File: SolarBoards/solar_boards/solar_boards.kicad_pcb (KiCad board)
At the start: 2 copper layers, 51.8 x 47 mm, 5 parts, among them J1 M55-6001242R

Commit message: boost converter values, will add solar cell
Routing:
- net (no net): track 0.00 -> 15.2 mm
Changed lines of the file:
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@@
 		(layer "Edge.Cuts")
+	)
+	(segment
+		(start 98 83.5)
+		(end 87 83.5)
+		(width 0.2)
+		(layer "F.Cu")
+		(net 0)
+	)
+	(segment
+		(start 87 83.5)
+		(end 84 86.5)
+		(width 0.2)
+		(layer "F.Cu")
+		(net 0)
 	)
 	(embedded_fonts no)

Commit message: Solar Board Schematic and Routing
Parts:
- added C1: 10uF, Capacitor_SMD:C_0402_1005Metric_Pad0.74x0.62mm_HandSolder, B.Cu at (89.1, 86.4)
- added C2: 10uF, Capacitor_SMD:C_0402_1005Metric_Pad0.74x0.62mm_HandSolder, B.Cu at (89.1, 87.8)
- added C3: 10uF, Capacitor_SMD:C_0402_1005Metric_Pad0.74x0.62mm_HandSolder, B.Cu at (93.7, 92.8)
- added C4: 1uF, Capacitor_SMD:C_0402_1005Metric_Pad0.74x0.62mm_HandSolder, B.Cu at (89.7, 93.8)
- added C5: 4.7uF, Capacitor_SMD:C_0402_1005Metric_Pad0.74x0.62mm_HandSolder, B.Cu at (83.5, 91.1)
- added C6: 10uF, Capacitor_SMD:C_0402_1005Metric_Pad0.74x0.62mm_HandSolder, B.Cu at (95.3, 92.8)
- added C7: 100nF, Capacitor_SMD:C_0402_1005Metric_Pad0.74x0.62mm_HandSolder, B.Cu at (96.9, 97.1)
- added C8: 1uF, Capacitor_SMD:C_0402_1005Metric_Pad0.74x0.62mm_HandSolder, B.Cu at (97.5, 92.8)
- added C9: 1uF, Capacitor_SMD:C_0402_1005Metric_Pad0.74x0.62mm_HandSolder, B.Cu at (101.2, 92.7)
- added D1: CDBQC0130L, inspireFly:DIODFN100X60X55-2N, F.Cu at (75.2, 74.5)
- added D2: CDBQC0130L, inspireFly:DIODFN100X60X55-2N, F.Cu at (84.6, 83.8)
- added D3: CDBQC0130L, inspireFly:DIODFN100X60X55-2N, F.Cu at (84.6, 92.6)
- added D4: CDBQC0130L, inspireFly:DIODFN100X60X55-2N, F.Cu at (84.6, 102.3)
- added D5: CDBQC0130L, inspireFly:DIODFN100X60X55-2N, F.Cu at (93.2, 76.0)
- added D6: CDBQC0130L, inspireFly:DIODFN100X60X55-2N, F.Cu at (99.2, 76.0)
- added L1: 10uH, inspireFly:WE-LQFS_3818, B.Cu at (94.0, 88.2)
- added R1: 332K, Resistor_SMD:R_0402_1005Metric_Pad0.72x0.64mm_HandSolder, B.Cu at (83.5, 89.6)
- added R2: 820K, Resistor_SMD:R_0402_1005Metric_Pad0.72x0.64mm_HandSolder, B.Cu at (91.4, 92.8)
- added R3: 200K, Resistor_SMD:R_0402_1005Metric_Pad0.72x0.64mm_HandSolder, B.Cu at (91.4, 95.6)
- added R4: 549K, Resistor_SMD:R_0402_1005Metric_Pad0.72x0.64mm_HandSolder, B.Cu at (98.0, 87.0)
- added R5: 200K, Resistor_SMD:R_0402_1005Metric_Pad0.72x0.64mm_HandSolder, B.Cu at (98.0, 84.8)
- added R6: 200K, Resistor_SMD:R_0402_1005Metric_Pad0.72x0.64mm_HandSolder, B.Cu at (102.1, 84.8)
- added R7: 820K, Resistor_SMD:R_0402_1005Metric_Pad0.72x0.64mm_HandSolder, B.Cu at (102.1, 87.0)
- added SC1: Solar_Cell, inspireFly:SOLAR_KXOB25-14X1F-TR, F.Cu at (71.8, 79.5)
- added SC2: Solar_Cell, inspireFly:SOLAR_KXOB25-14X1F-TR, F.Cu at (71.8, 88.2)
- added SC3: Solar_Cell, inspireFly:SOLAR_KXOB25-14X1F-TR, F.Cu at (71.7, 96.8)
- added SC4: Solar_Cell, inspireFly:SOLAR_KXOB25-14X1F-TR, F.Cu at (71.5, 105.5)
- added SC5: Solar_Cell, inspireFly:SOLAR_KXOB25-14X1F-TR, F.Cu at (97.8, 81.4)
- added SC6: Solar_Cell, inspireFly:SOLAR_KXOB25-14X1F-TR, F.Cu at (97.8, 104.2)
- added U1: LTC3105EDD-TRPBF, inspireFly:DFN-10_DD_LIT, B.Cu at (88.2, 90.6)
- added U2: OPT3004DNPR, inspireFly:DNP0006A, F.Cu at (99.0, 95.1)
- added U3: LM73100RPWR, inspireFly:IC_LM73100RPWR, B.Cu at (99.9, 90.1)
- moved J1 0.61 mm to (108.1, 92.6), turned to -90 degrees
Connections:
- J1 pad A1: unconnected-(J1-PadA1) -> GND
- J1 pad A2: unconnected-(J1-PadA2) -> GND
- J1 pad A3: unconnected-(J1-PadA3) -> GND
- J1 pad A4: unconnected-(J1-PadA4) -> GND
- J1 pad A5: unconnected-(J1-PadA5) -> GND
- J1 pad A6: unconnected-(J1-PadA6) -> GND
- J1 pad B1: unconnected-(J1-PadB1) -> EXTERNAL_VOLTAGE
- J1 pad B2: unconnected-(J1-PadB2) -> EXTERNAL_VOLTAGE
- J1 pad B3: unconnected-(J1-PadB3) -> EXTERNAL_VOLTAGE
- J1 pad B4: unconnected-(J1-PadB4) -> EXTERNAL_VOLTAGE
- J1 pad B5: unconnected-(J1-PadB5) -> I2C_SCL
- J1 pad B6: unconnected-(J1-PadB6) -> I2C_SDA
- J1 pad SH1: unconnected-(J1-PadSH1) -> GND
- J1 pad SH2: unconnected-(J1-PadSH2) -> GND
- J1 pad SH3: unconnected-(J1-PadSH3) -> GND
- J1 pad SH4: unconnected-(J1-PadSH4) -> GND
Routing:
- net Net-(D1-K): track 0.00 -> 50.2 mm, vias 0 -> 1
- net Net-(D5-A): track 0.00 -> 50.1 mm
- net Net-(D1-A): track 0.00 -> 38.1 mm
- net Net-(D4-A): track 0.00 -> 36.0 mm
- net Net-(D3-A): track 0.00 -> 35.6 mm
- net Net-(D2-A): track 0.00 -> 34.8 mm
- net +2.2V: track 0.00 -> 26.4 mm, vias 0 -> 1
- net (no net): track 15.2 -> 0.00 mm
- net Net-(U1-FB): track 0.00 -> 10.6 mm
- net Net-(U1-VOUT): track 0.00 -> 7.93 mm
- net Net-(U1-SW): track 0.00 -> 6.72 mm
- net I2C_SDA: track 0.00 -> 5.91 mm, vias 0 -> 1
- net I2C_SCL: track 0.00 -> 5.91 mm, vias 0 -> 1
- net Net-(U3-OVLO): track 0.00 -> 5.72 mm
- net Net-(U3-EN/UVLO): track 0.00 -> 4.66 mm
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- added copper zone on B.Cu, net EXTERNAL_VOLTAGE
- added copper zone on B.Cu, net GND
- added copper zone on F.Cu, net GND
- added copper zone on B.Cu, net Net-(U1-VOUT)
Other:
- board size 51.8 x 47 mm -> 52.8 x 47 mm

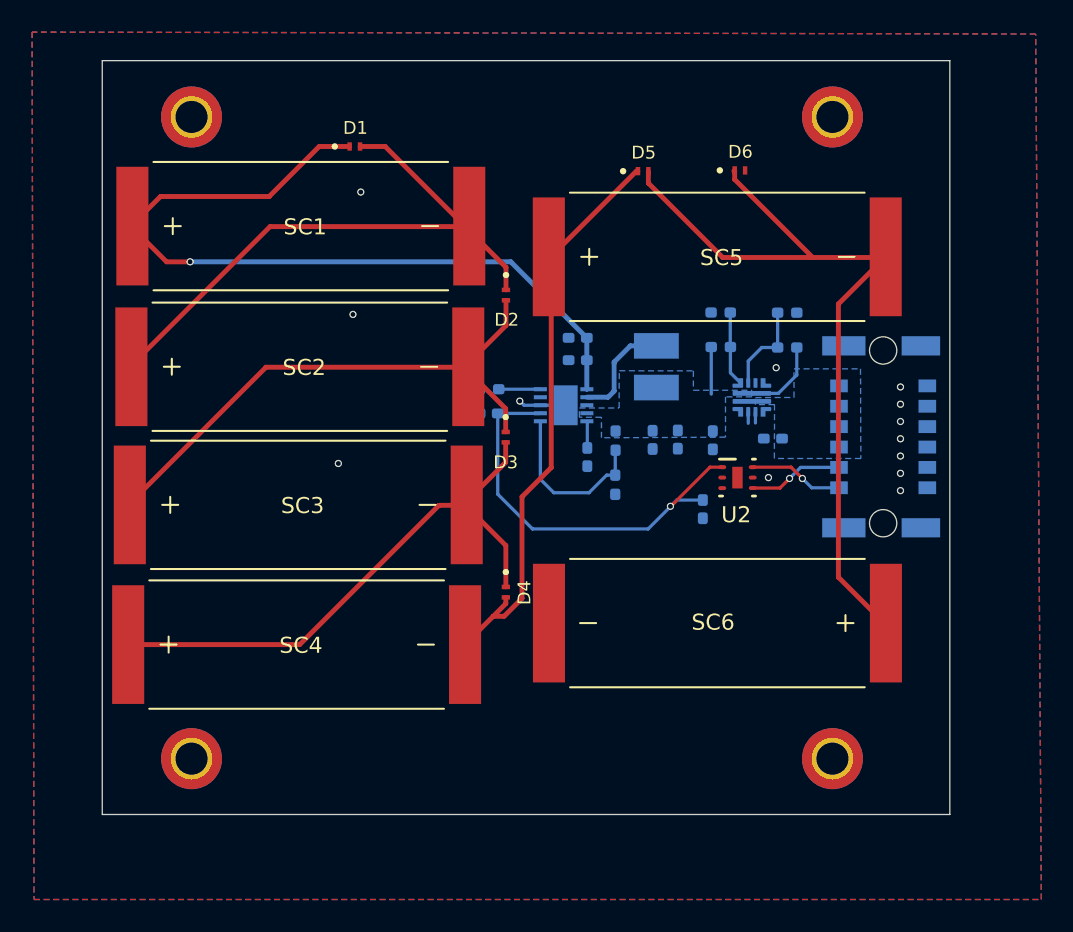
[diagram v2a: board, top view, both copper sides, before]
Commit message: Routing and schematic work on most boards
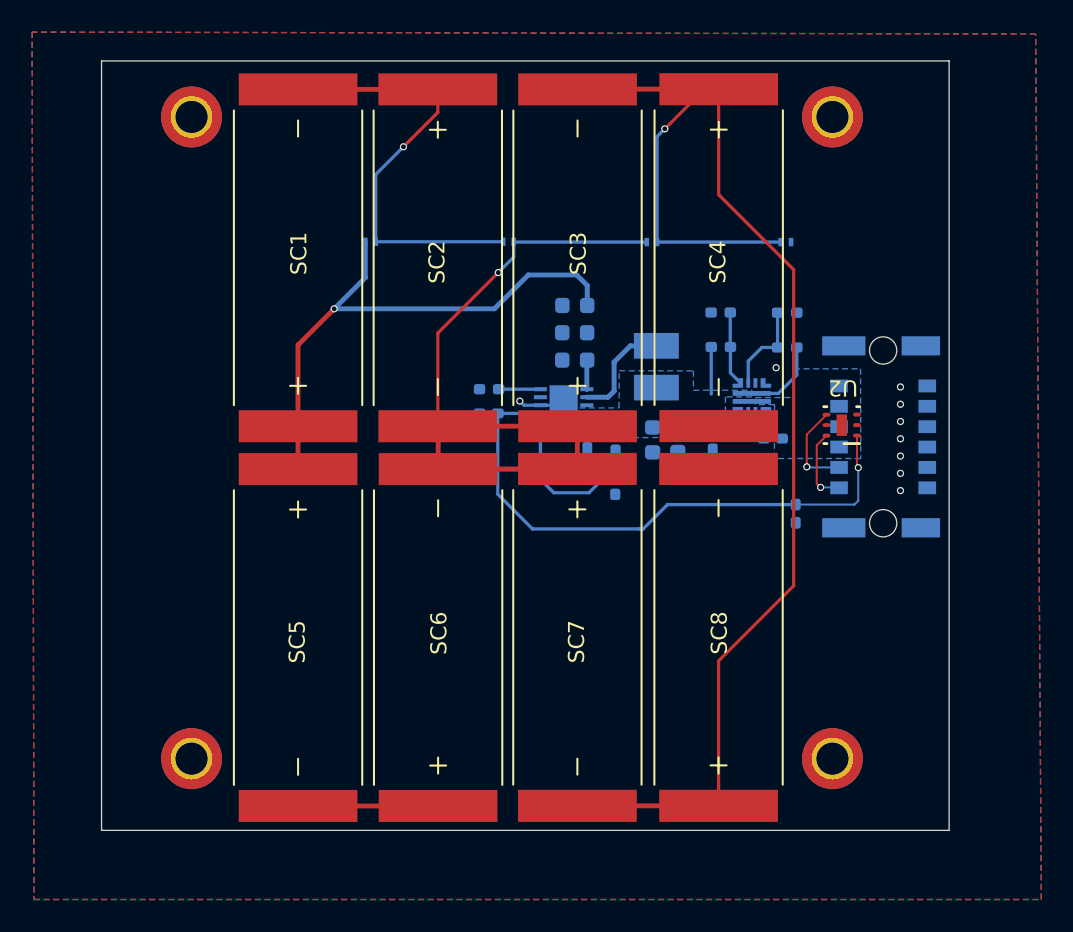
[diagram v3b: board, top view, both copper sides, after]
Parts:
- removed D5, D6: CDBQC0130L, inspireFly:DIODFN100X60X55-2N
- added C10: 10uF, Capacitor_SMD:C_0603_1608Metric, B.Cu at (88.9, 84.4)
- added SC7: Solar_Cell, inspireFly:SOLAR_KXOB25-14X1F-TR, F.Cu at (89.0, 105.1)
- added SC8: Solar_Cell, inspireFly:SOLAR_KXOB25-14X1F-TR, F.Cu at (97.8, 105.1)
- C1, C2, C3, C6: footprint Capacitor_SMD:C_0402_1005Metric_Pad0.74x0.62mm_HandSolder -> Capacitor_SMD:C_0603_1608Metric
- D1, D2, D3, D4: moved to B.Cu
- R1: value 332K -> 215K
- moved SC4 35.7 mm to (97.9, 81.4), turned to -90 degrees
- moved SC5 35.3 mm to (71.6, 105.1), turned to -90 degrees
- moved D4 27.9 mm to (102.0, 80.5), turned to 0 degrees
- moved SC3 23.2 mm to (89.1, 81.4), turned to 90 degrees
- moved SC6 17.4 mm to (80.4, 105.1), turned to 90 degrees
- moved D3 15.2 mm to (93.7, 80.5), turned to 0 degrees
- moved SC2 11.0 mm to (80.3, 81.4), turned to -90 degrees
- moved U2 7.28 mm to (105.5, 91.9), turned to 180 degrees
- moved D1 6.02 mm to (76.2, 80.4)
- moved C7 5.80 mm to (102.7, 97.4)
- moved D2 3.33 mm to (84.8, 80.4), turned to 0 degrees
- moved SC1 1.98 mm to (71.6, 81.4), turned to 90 degrees
- moved C1 0.37 mm to (88.9, 86.1)
- moved C2 0.19 mm to (88.9, 87.8)
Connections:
- D4 pad 2: Net-(D4-A) -> GND
- SC4 pad 2: Net-(D4-A) -> GND
- SC5 pad 1: Net-(D4-A) -> Net-(D1-K)
- SC5 pad 2: Net-(D5-A) -> Net-(D1-A)
- SC6 pad 1: Net-(D5-A) -> Net-(D1-A)
- SC6 pad 2: GND -> Net-(D2-A)
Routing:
- net Net-(D5-A): track 50.1 -> 0.00 mm
- net Net-(D3-A): track 35.6 -> 85.5 mm, vias 0 -> 1
- net Net-(D4-A): track 36.0 -> 0.00 mm
- net Net-(D1-K): track 50.2 -> 35.9 mm
- net Net-(D2-A): track 34.8 -> 44.5 mm, vias 0 -> 1
- net +2.2V: track 26.4 -> 35.9 mm
- net Net-(D1-A): track 38.1 -> 36.5 mm, vias 0 -> 1
- net I2C_SDA: track 5.91 -> 4.74 mm
- net GND: track 4.25 -> 5.01 mm, vias 13 -> 9
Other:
- board size 52.8 x 47 mm -> 52.8 x 48 mm

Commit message: Finalize board work + BOM work
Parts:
- added G***: LOGO, LOGO, B.Cu at (85.6, 102.7)
- C5: footprint Capacitor_SMD:C_0402_1005Metric_Pad0.74x0.62mm_HandSolder -> Capacitor_SMD:C_0603_1608Metric
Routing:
- net Net-(D1-A): track 36.5 -> 85.9 mm
- net Net-(D1-K): track 35.9 -> 39.3 mm
- net GND: vias 9 -> 14
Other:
- board text added: "Solar Board PQ V0.1"
